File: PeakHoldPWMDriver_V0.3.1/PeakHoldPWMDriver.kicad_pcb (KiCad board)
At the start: 2 copper layers, 100.1 x 50 mm, 116 parts, among them J1 RND 205-00203, J2 RND 205-00205, Q1 2N7002, Q10 2N7002, Q11 2N7002, Q12 2N7002, Q13 TSM2309, Q14 IRLL 024N, Q15 TSM2309, Q16 IRLL 024N, Q17 TSM2309, Q18 TSM2309, Q19 TSM2309, Q2 2N7002, Q20 TSM2309, Q3 2N7002, Q4 2N7002, Q5 TSM2309, Q6 TSM2309, Q7 IRLL 024N, Q8 IRLL 024N, Q9 2N7002, U1 74LS32, U2 LM2901, U3 74LS74, U4 LTC6992, U5 74LS74, U6 LM340, U7 74LS08, U8 74LS08

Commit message: Changed resistor value R5, now correct PWM freqency
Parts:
- R5: value 28k -> 15k
- U1: value 74LS32 -> 74HC32
- U3, U5: value 74LS74 -> 74HC74
- U7, U8: value 74LS08 -> 74HC08

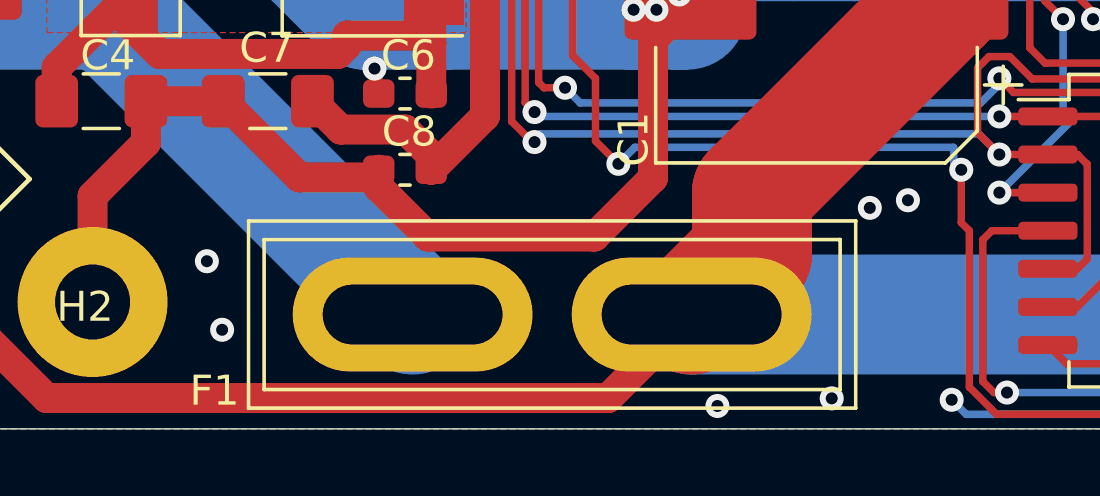
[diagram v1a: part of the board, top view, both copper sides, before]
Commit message: Update schematic for clarity
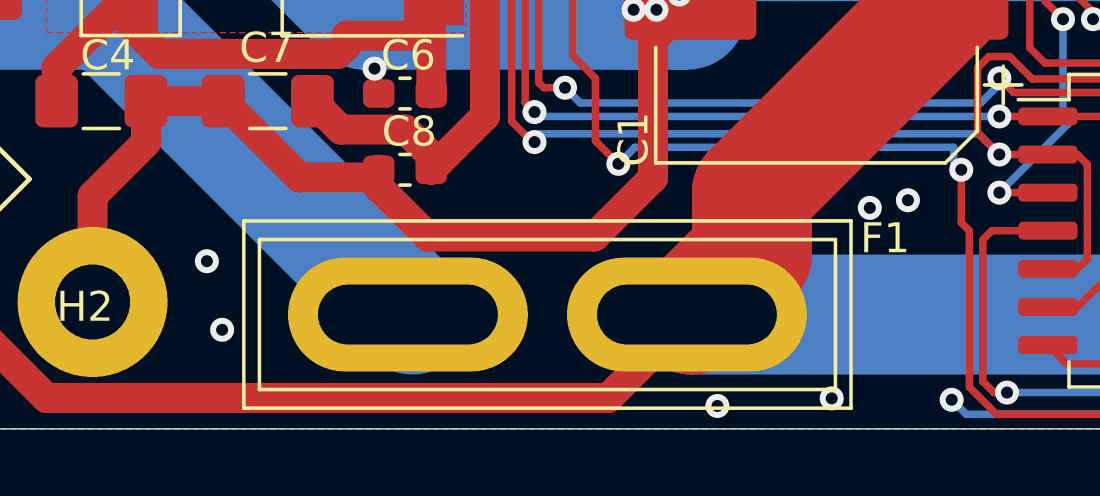
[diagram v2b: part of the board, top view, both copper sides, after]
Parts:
- moved F1 9.14 mm to (145.5, 112.3), turned to 180 degrees
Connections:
- F1 pad 1: VBAT_IN -> VBAT
- F1 pad 2: VBAT -> VBAT_IN
